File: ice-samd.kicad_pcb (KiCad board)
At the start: 2 copper layers, 50.8 x 22.9 mm, 30 parts, among them J1 Conn_Battery, J2 USB_B_Micro, J3 Conn_Left, J4 Conn_Right, U1 SPX3819M5-L-3-3, U2 ATSAMD21G18A-AUT, U3 MCP73831-2-OT, Y1 32.768

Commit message: Updated samd21
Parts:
- added IC1: ADXL345, ADX:ADXL3x5, F.Cu at (163.2, 93.3)
- added R7: 10k, Resistor_SMD:R_0603_1608Metric, F.Cu at (172.2, 84.6)
- added R8: 10k, Resistor_SMD:R_0603_1608Metric, F.Cu at (168.1, 84.6)
- added U4: ATECC608A-MAHDA, Package_DFN_QFN:DFN-8-1EP_3x2mm_P0.5mm_EP1.3x1.5mm, F.Cu at (161.6, 87.6)
- TP1, TP2: moved to B.Cu
- moved D1 50.3 mm to (150.4, 86.0), turned to 90 degrees
- moved R3 49.9 mm to (144.9, 86.1), turned to 270 degrees
- moved Y1 45.9 mm to (137.8, 99.5), turned to 90 degrees
- moved R1 43.4 mm to (158.8, 95.9), turned to 270 degrees
- moved C6 42.5 mm to (137.0, 94.5), turned to 90 degrees
- moved TP1 42.1 mm to (133.3, 100.4), turned to 270 degrees
- moved C5 41.6 mm to (134.3, 97.9), turned to 270 degrees
- moved R4 41.3 mm to (156.6, 95.9), turned to 90 degrees
- moved C3 41.1 mm to (153.8, 95.9), turned to 270 degrees
- moved TP2 39.4 mm to (135.9, 100.4), turned to 270 degrees
- moved D3 37.2 mm to (152.5, 92.5), turned to 270 degrees
- moved C7 33.1 mm to (152.3, 86.1), turned to 270 degrees
- moved R5 32.6 mm to (155.9, 86.1), turned to 270 degrees
- moved C2 30.7 mm to (150.8, 92.5), turned to 90 degrees
- moved R6 28.1 mm to (158.3, 92.3), turned to 90 degrees
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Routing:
- net GND: track 22.5 -> 97.5 mm, vias 0 -> 7
- net /SDA: track 0.00 -> 53.0 mm, vias 0 -> 3
- net +3V3: track 10.4 -> 55.8 mm, vias 0 -> 13
- net /SCL: track 0.00 -> 42.4 mm, vias 0 -> 5
- net /D13: track 0.00 -> 33.3 mm, vias 0 -> 3
- net /D9: track 0.00 -> 31.9 mm, vias 0 -> 7
- net +BATT: track 2.74 -> 32.0 mm, vias 0 -> 2
- net Net-(C4-Pad2): track 0.00 -> 27.0 mm, vias 0 -> 4
- net /A5: track 0.00 -> 26.8 mm, vias 0 -> 1
- net /D6: track 0.00 -> 26.7 mm, vias 0 -> 4
- net /D5: track 0.00 -> 25.6 mm
- net /D1: track 0.00 -> 24.5 mm, vias 0 -> 3
- net /D0: track 0.00 -> 23.9 mm, vias 0 -> 2
- net /MOSI: track 0.00 -> 23.0 mm
- net VBUS: track 23.2 -> 46.0 mm, vias 1 -> 5
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
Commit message: Updated LED locations
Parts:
- moved R4 26.3 mm to (132.0, 86.5), turned to 270 degrees
- moved D3 23.8 mm to (129.4, 98.4), turned to 0 degrees
- moved D2 17.5 mm to (129.2, 87.0), turned to 180 degrees
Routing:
- net Net-(D2-Pad1): track 2.87 -> 19.3 mm, vias 0 -> 2
- net GND: track 97.5 -> 109.2 mm, vias 7 -> 9
- net Net-(D3-Pad2): track 5.38 -> 14.0 mm, vias 0 -> 2
- net /D13: track 33.3 -> 41.8 mm, vias 3 -> 5
- net +3V3: track 55.8 -> 49.3 mm
- net VBUS: track 46.0 -> 52.1 mm
- net /SDA: track 53.0 -> 49.7 mm
- net Net-(R2-Pad1): track 21.5 -> 20.2 mm
- net +BATT: track 32.0 -> 33.2 mm
- net Net-(R3-Pad2): track 16.1 -> 14.9 mm
- net /D6: track 26.7 -> 27.8 mm

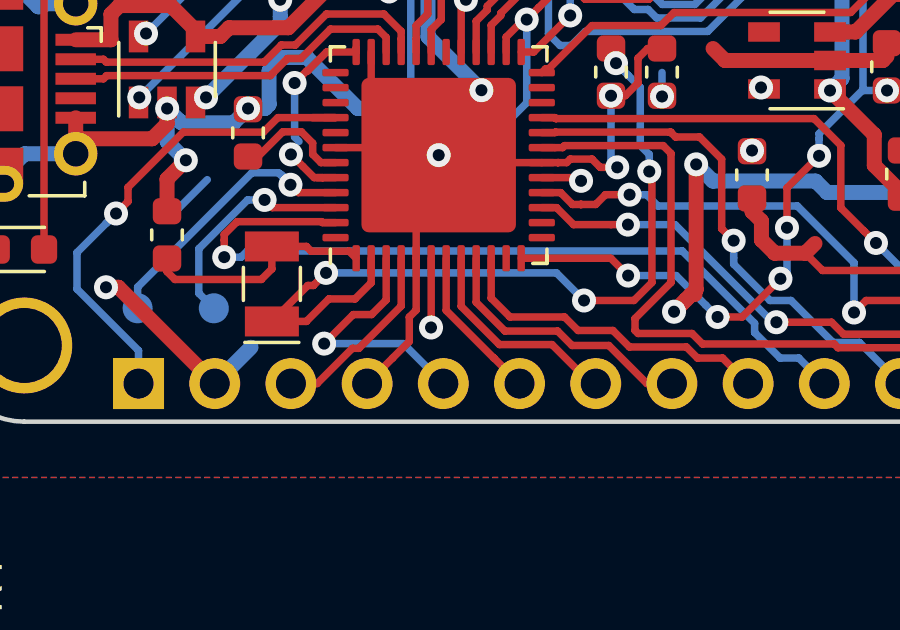
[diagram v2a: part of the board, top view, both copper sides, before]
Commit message: cleaned up traces
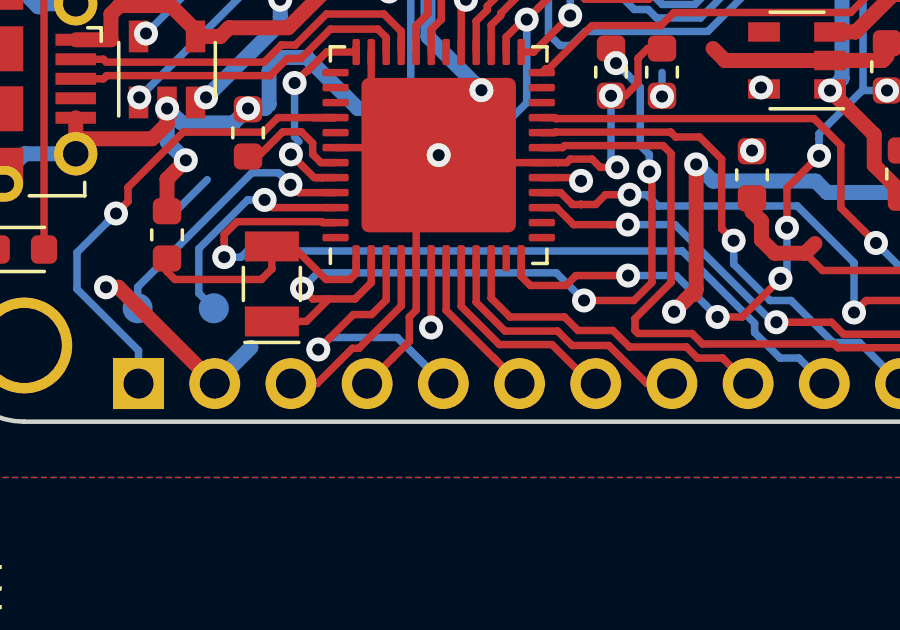
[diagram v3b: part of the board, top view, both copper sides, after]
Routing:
- net /A0: track 8.91 -> 11.5 mm
- net Net-(C5-Pad2): track 7.91 -> 8.79 mm
- net /D9: track 31.9 -> 32.6 mm
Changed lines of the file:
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@@
     (thickness 1.6)
     (drawings 14)
-    (tracks 780)
+    (tracks 790)
     (zones 0)
     (modules 34)
@@
   (segment (start 141.605 100.084251) (end 141.119261 100.56999) (width 0.25) (layer F.Cu) (net 13))
   (segment (start 141.605 98.6925) (end 141.605 100.084251) (width 0.25) (layer F.Cu) (net 13))
-  (via (at 139.537838 101.537838) (size 0.8) (drill 0.4) (layers F.Cu B.Cu) (net 13))
   (segment (start 141.119261 100.56999) (end 140.505686 100.56999) (width 0.25) (layer F.Cu) (net 13))
   (segment (start 140.505686 100.56999) (end 139.537838 101.537838) (width 0.25) (layer F.Cu) (net 13))
   (segment (start 142.177838 101.537838) (end 143.51 102.87) (width 0.25) (layer B.Cu) (net 13))
-  (segment (start 139.537838 101.537838) (end 142.177838 101.537838) (width 0.25) (layer B.Cu) (net 13))
-  (segment (start 142.105 100.285585) (end 140.695586 101.694999) (width 0.25) (layer F.Cu) (net 14))
-  (segment (start 142.105 98.6925) (end 142.105 100.285585) (width 0.25) (layer F.Cu) (net 14))
+  (via (at 139.341916 101.733762) (size 0.8) (drill 0.4) (layers F.Cu B.Cu) (net 13))
+  (segment (start 139.537838 101.53784) (end 139.341916 101.733762) (width 0.25) (layer F.Cu) (net 13))
+  (segment (start 139.537838 101.537838) (end 139.537838 101.53784) (width 0.25) (layer F.Cu) (net 13))
+  (segment (start 142.660001 102.020001) (end 143.51 102.87) (width 0.25) (layer B.Cu) (net 13))
+  (segment (start 141.973763 101.333763) (end 142.660001 102.020001) (width 0.25) (layer B.Cu) (net 13))
+  (segment (start 139.741915 101.333763) (end 141.973763 101.333763) (width 0.25) (layer B.Cu) (net 13))
+  (segment (start 139.341916 101.733762) (end 139.741915 101.333763) (width 0.25) (layer B.Cu) (net 13))
   (segment (start 140.478005 101.694999) (end 139.303004 102.87) (width 0.25) (layer F.Cu) (net 14))
   (segment (start 139.303004 102.87) (end 138.43 102.87) (width 0.25) (layer F.Cu) (net 14))
   (segment (start 140.695586 101.694999) (end 140.478005 101.694999) (width 0.25) (layer F.Cu) (net 14))
+  (segment (start 142.105 100.285585) (end 140.695586 101.694999) (width 0.25) (layer F.Cu) (net 14))
+  (segment (start 142.105 98.6925) (end 142.105 100.285585) (width 0.25) (layer F.Cu) (net 14))
   (via (at 154.1 93) (size 0.8) (drill 0.4) (layers F.Cu B.Cu) (net 15))
   (via (at 150.8 93.3) (size 0.8) (drill 0.4) (layers F.Cu B.Cu) (net 15))
@@
   (segment (start 144.105 90.233498) (end 144.26216 90.076338) (width 0.25) (layer F.Cu) (net 25))
   (via (at 158.3 93.1) (size 0.8) (drill 0.4) (layers F.Cu B.Cu) (net 26))
-  (segment (start 146.105 98.6925) (end 149.0925 98.6925) (width 0.25) (layer F.Cu) (net 26))
   (via (at 149.669835 99.269835) (size 0.8) (drill 0.4) (layers F.Cu B.Cu) (net 26))
-  (segment (start 149.0925 98.6925) (end 149.669835 99.269835) (width 0.25) (layer F.Cu) (net 26))
   (segment (start 157.527325 93.1) (end 157.5 93.072675) (width 0.25) (layer B.Cu) (net 26))
   (segment (start 158.3 93.1) (end 157.527325 93.1) (width 0.25) (layer B.Cu) (net 26))
@@
   (segment (start 157.5 93.072675) (end 157.5 87.680297) (width 0.25) (layer B.Cu) (net 26))
   (segment (start 157.5 87.680297) (end 157.10971 87.290007) (width 0.25) (layer B.Cu) (net 26))
+  (segment (start 146.105 98.6925) (end 146.105 99.295) (width 0.25) (layer F.Cu) (net 26))
+  (segment (start 146.105 99.295) (end 146.41 99.6) (width 0.25) (layer F.Cu) (net 26))
+  (segment (start 146.41 99.6) (end 147.6 99.6) (width 0.25) (layer F.Cu) (net 26))
+  (segment (start 147.930165 99.269835) (end 149.669835 99.269835) (width 0.25) (layer F.Cu) (net 26))
+  (segment (start 147.6 99.6) (end 147.930165 99.269835) (width 0.25) (layer F.Cu) (net 26))
   (segment (start 152.085283 90.681244) (end 150.617655 90.681244) (width 0.25) (layer B.Cu) (net 27))
   (segment (start 149.191518 89.716837) (end 148.791519 89.316838) (width 0.25) (layer B.Cu) (net 27))
@@
   (segment (start 141.105 99.178022) (end 141.105 99.13) (width 0.25) (layer F.Cu) (net 47))
   (segment (start 141.105 99.13) (end 141.105 98.6925) (width 0.25) (layer F.Cu) (net 47))
-  (segment (start 138.993 99.6) (end 137.795 100.798) (width 0.25) (layer F.Cu) (net 47))
   (segment (start 138.945 100.798) (end 139.695 100.048) (width 0.25) (layer F.Cu) (net 47))
   (segment (start 141.105 99.511249) (end 141.105 99.13) (width 0.25) (layer F.Cu) (net 47))
@@
   (segment (start 140.568249 100.048) (end 141.105 99.511249) (width 0.25) (layer F.Cu) (net 47))
   (segment (start 139.695 100.048) (end 140.568249 100.048) (width 0.25) (layer F.Cu) (net 47))
-  (segment (start 139.18002 99.6) (end 139.6 99.18002) (width 0.25) (layer F.Cu) (net 47))
-  (segment (start 138.993 99.6) (end 139.18002 99.6) (width 0.25) (layer F.Cu) (net 47))
-  (via (at 139.6 99.18002) (size 0.8) (drill 0.4) (layers F.Cu B.Cu) (net 47))
   (via (at 150.37499 95.8) (size 0.8) (drill 0.4) (layers F.Cu B.Cu) (net 47))
   (via (at 148.2 100.1) (size 0.8) (drill 0.4) (layers F.Cu B.Cu) (net 47))
@@
   (segment (start 149.265693 91.865693) (end 149.1 91.7) (width 0.25) (layer F.Cu) (net 47))
   (segment (start 149.265693 92.189354) (end 149.265693 91.865693) (width 0.25) (layer F.Cu) (net 47))
-  (segment (start 139.10201 98.45501) (end 138.945 98.298) (width 0.25) (layer F.Cu) (net 48))
-  (segment (start 138.945 98.298) (end 137.795 98.298) (width 0.25) (layer F.Cu) (net 48))
-  (segment (start 140.605 98.6925) (end 140.36751 98.45501) (width 0.25) (layer F.Cu) (net 48))
-  (segment (start 140.36751 98.45501) (end 139.10201 98.45501) (width 0.25) (layer F.Cu) (net 48))
+  (via (at 138.8 99.7) (size 0.8) (drill 0.4) (layers F.Cu B.Cu) (net 47))
+  (segment (start 139.6 99.18002) (end 139.31998 99.18002) (width 0.25) (layer B.Cu) (net 47))
+  (segment (start 139.31998 99.18002) (end 138.8 99.7) (width 0.25) (layer B.Cu) (net 47))
+  (segment (start 139.148 100.048) (end 139.695 100.048) (width 0.25) (layer F.Cu) (net 47))
+  (segment (start 138.8 99.7) (end 139.148 100.048) (width 0.25) (layer F.Cu) (net 47))
   (segment (start 137.795 99.048) (end 137.443 99.4) (width 0.25) (layer F.Cu) (net 48))
   (segment (start 137.795 98.298) (end 137.795 99.048) (width 0.25) (layer F.Cu) (net 48))
@@
   (segment (start 134.5625 99.4) (end 134.3 99.1375) (width 0.25) (layer F.Cu) (net 48))
   (segment (start 137.443 99.4) (end 134.5625 99.4) (width 0.25) (layer F.Cu) (net 48))
+  (segment (start 138.498 98.298) (end 137.795 98.298) (width 0.25) (layer F.Cu) (net 48))
+  (segment (start 139.6 99.4) (end 138.498 98.298) (width 0.25) (layer F.Cu) (net 48))
+  (segment (start 140.4 99.4) (end 139.6 99.4) (width 0.25) (layer F.Cu) (net 48))
+  (segment (start 140.605 98.6925) (end 140.605 99.195) (width 0.25) (layer F.Cu) (net 48))
+  (segment (start 140.605 99.195) (end 140.4 99.4) (width 0.25) (layer F.Cu) (net 48))
   (via (at 133.6 91.2) (size 0.8) (drill 0.4) (layers F.Cu B.Cu) (net 49))
   (segment (start 133.35 91.3) (end 133.5 91.3) (width 0.25) (layer F.Cu) (net 49))
